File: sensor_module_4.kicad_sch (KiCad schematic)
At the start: 34 parts, among them J1 pH_IN, J17 Atlas Surveyor, J18 EZO Carrier Board, J3 ORP_In, J4 Turbidity TSW-10, U3 ESDA5V3SC5, U4 OPA2397DGKR, U5 OPA2397DGKR

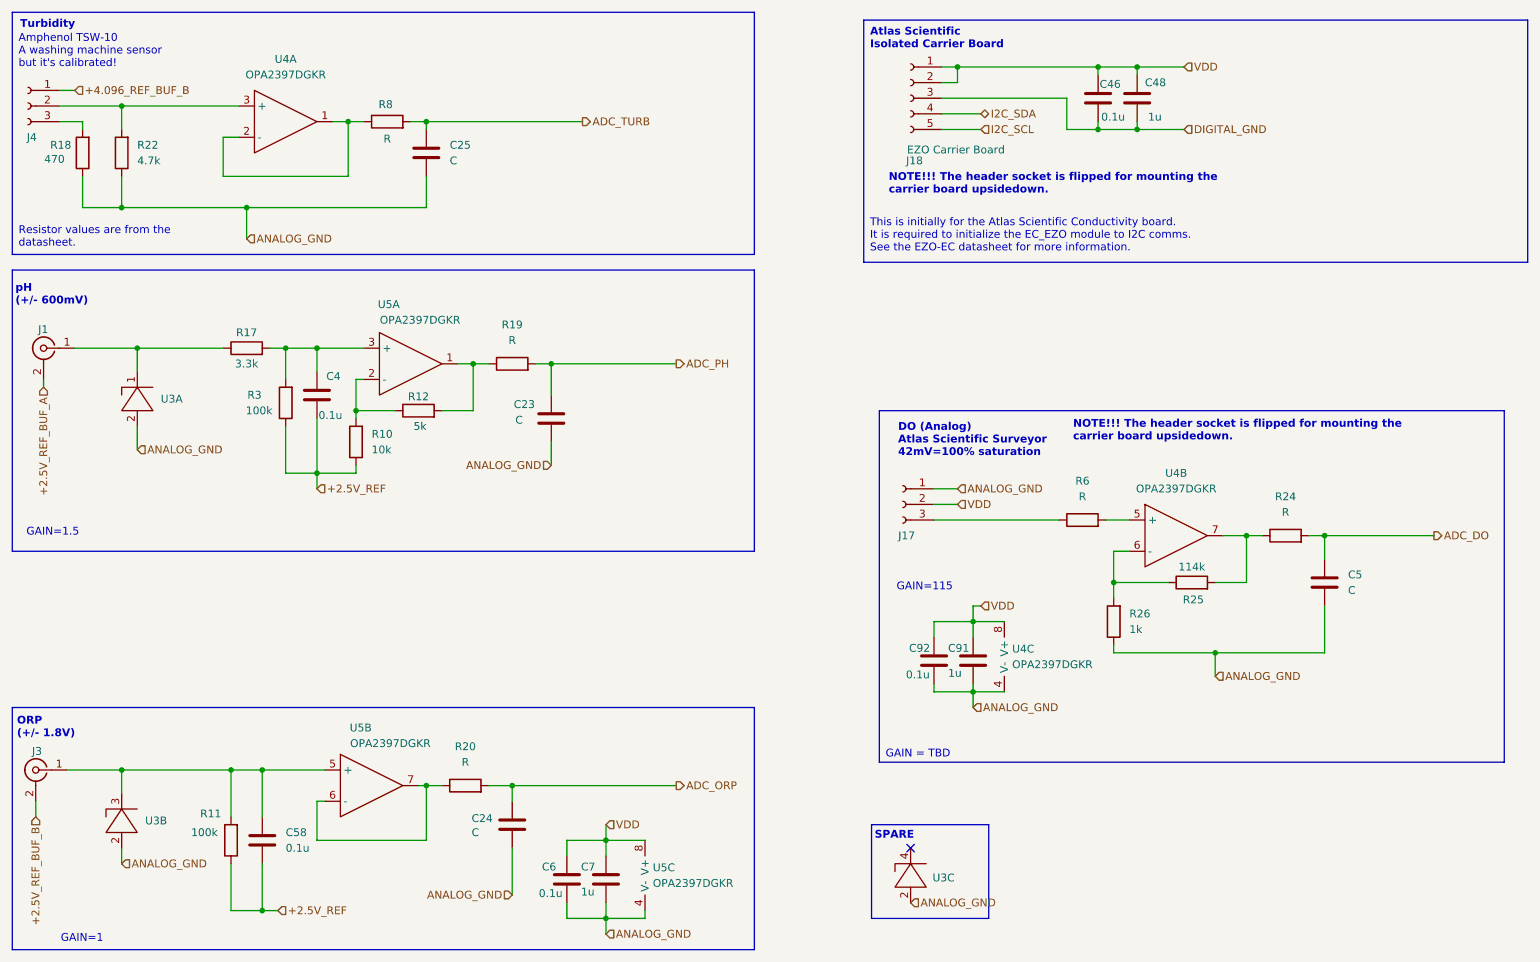
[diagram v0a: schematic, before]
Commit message: BUG_FIX ------- - Swapped ground for the 2.5V reference on the non-inverting leg of U11B (External temperature probe)   This is due to the fact that the temp probe voltage can go both above and below the reference point so we need something higher than ground to prevent pegging the output to 0 when temp probe impedance drops below 1k.
FEATURES
--------
- Finalized many of the parts for the BOM
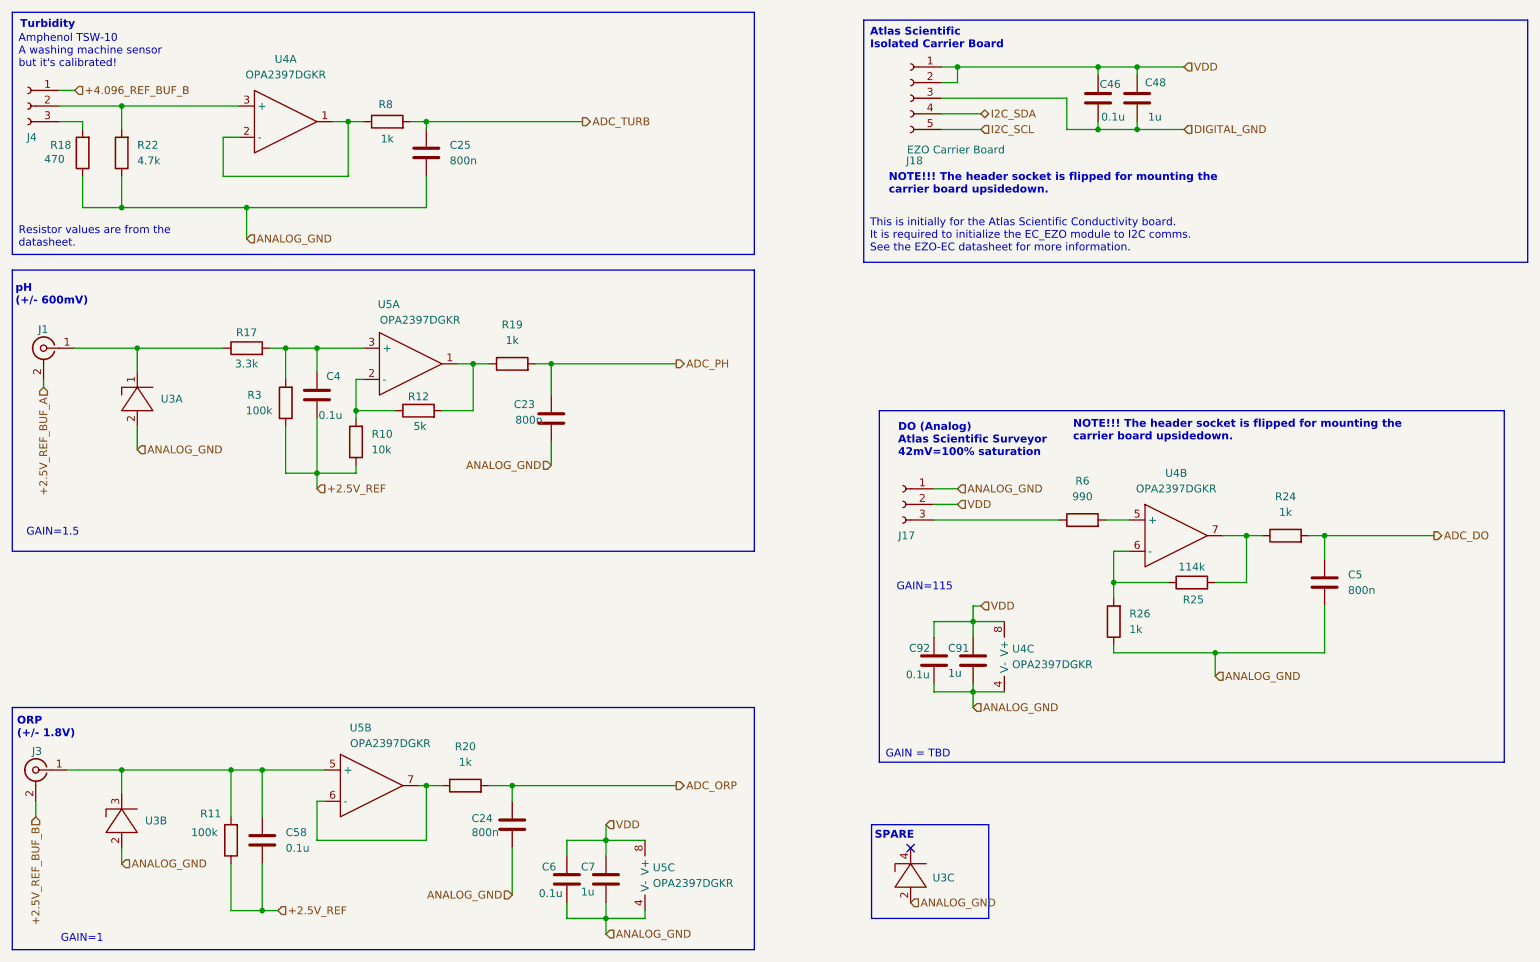
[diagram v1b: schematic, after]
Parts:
- C23, C24, C25, C5: value C -> 800n
- R19, R20, R24, R8: value R -> 1k
- R6: value R -> 990
